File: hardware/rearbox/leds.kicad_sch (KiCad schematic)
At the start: 16 parts

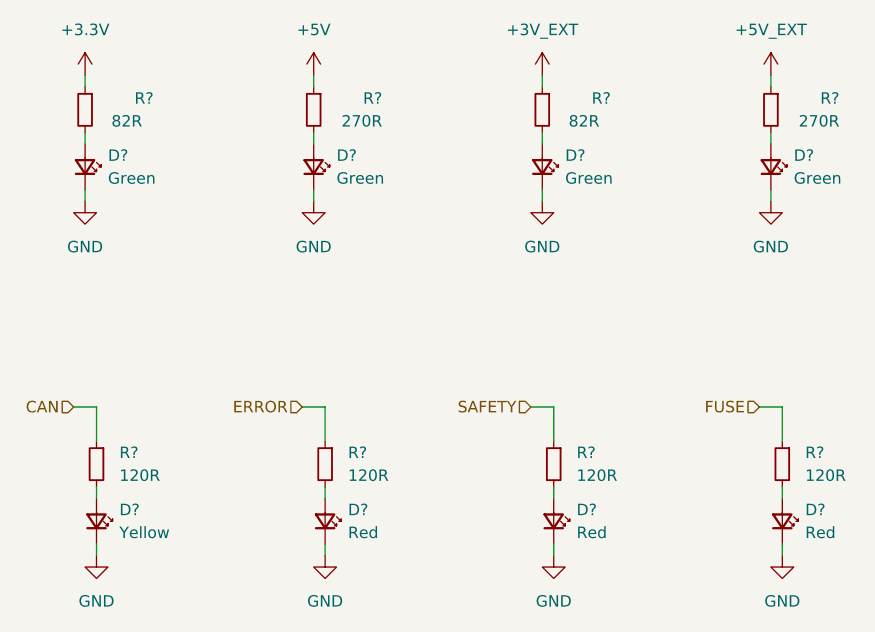
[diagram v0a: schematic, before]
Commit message: Place components on the PCB
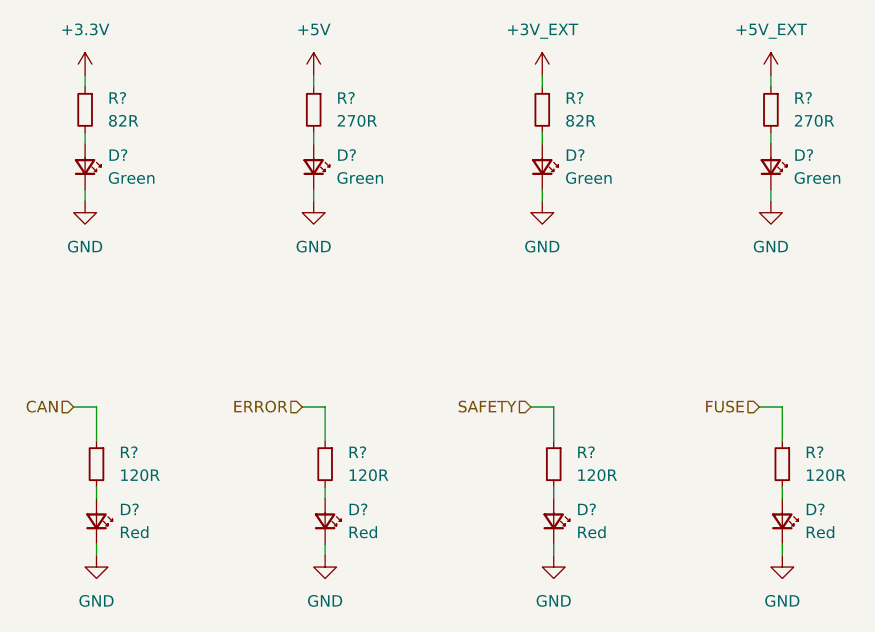
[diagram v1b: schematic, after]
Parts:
- D?: value Yellow -> Red
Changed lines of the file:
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@@
   (title_block
     (title "LEDs")
-    (date "2023-10-01")
+    (date "2023-11-02")
     (rev "${REVISION}")
     (company "Author: I. Kajdan")
@@
         )
         (path "/b652b05a-4e3d-4ad1-b032-18886abe7d45/6999686b-4026-4ea7-9227-634603a79198"
-          (reference "#PWR098") (unit 1)
+          (reference "#PWR095") (unit 1)
         )
       )
@@
         )
         (path "/b652b05a-4e3d-4ad1-b032-18886abe7d45/6999686b-4026-4ea7-9227-634603a79198"
-          (reference "#PWR099") (unit 1)
+          (reference "#PWR096") (unit 1)
         )
       )
@@
         )
         (path "/b652b05a-4e3d-4ad1-b032-18886abe7d45/6999686b-4026-4ea7-9227-634603a79198"
-          (reference "#PWR0106") (unit 1)
+          (reference "#PWR0103") (unit 1)
         )
       )
@@
         )
         (path "/b652b05a-4e3d-4ad1-b032-18886abe7d45/6999686b-4026-4ea7-9227-634603a79198"
-          (reference "R61") (unit 1)
+          (reference "R35") (unit 1)
         )
       )
@@
   (symbol (lib_id "Device:R_Small") (at 186.69 76.2 0) (mirror y) (unit 1)
     (in_bom yes) (on_board yes) (dnp no)
-    (property "Reference" "R?" (at 194.31 74.93 0)
-      (effects (font (size 1.27 1.27)) (justify left))
-    )
-    (property "Value" "270R" (at 194.31 77.47 0)
-      (effects (font (size 1.27 1.27)) (justify left))
+    (property "Reference" "R?" (at 189.23 74.93 0)
+      (effects (font (size 1.27 1.27)) (justify right))
+    )
+    (property "Value" "270R" (at 189.23 77.47 0)
+      (effects (font (size 1.27 1.27)) (justify right))
     )
     (property "Footprint" "Resistor_SMD:R_0603_1608Metric" (at 186.69 76.2 0)
@@
         )
         (path "/b652b05a-4e3d-4ad1-b032-18886abe7d45/6999686b-4026-4ea7-9227-634603a79198"
-          (reference "R66") (unit 1)
+          (reference "R40") (unit 1)
         )
       )
@@
       (effects (font (size 1.27 1.27)) (justify left))
     )
-    (property "Value" "Yellow" (at 114.3 123.19 90)
+    (property "Value" "Red" (at 114.3 123.19 90)
       (effects (font (size 1.27 1.27)) (justify left))
     )
@@
   (symbol (lib_id "Device:R_Small") (at 110.49 76.2 0) (mirror y) (unit 1)
     (in_bom yes) (on_board yes) (dnp no)
-    (property "Reference" "R?" (at 118.11 74.93 0)
-      (effects (font (size 1.27 1.27)) (justify left))
-    )
-    (property "Value" "82R" (at 116.84 77.47 0)
-      (effects (font (size 1.27 1.27)) (justify left))
+    (property "Reference" "R?" (at 113.03 74.93 0)
+      (effects (font (size 1.27 1.27)) (justify right))
+    )
+    (property "Value" "82R" (at 113.03 77.47 0)
+      (effects (font (size 1.27 1.27)) (justify right))
     )
     (property "Footprint" "Resistor_SMD:R_0603_1608Metric" (at 110.49 76.2 0)
@@
         )
         (path "/b652b05a-4e3d-4ad1-b032-18886abe7d45/6999686b-4026-4ea7-9227-634603a79198"
-          (reference "R60") (unit 1)
+          (reference "R34") (unit 1)
         )
       )
@@
         )
         (path "/b652b05a-4e3d-4ad1-b032-18886abe7d45/6999686b-4026-4ea7-9227-634603a79198"
-          (reference "#PWR096") (unit 1)
+          (reference "#PWR093") (unit 1)
         )
       )
@@
   (symbol (lib_id "Device:R_Small") (at 135.89 76.2 0) (mirror y) (unit 1)
     (in_bom yes) (on_board yes) (dnp no)
-    (property "Reference" "R?" (at 143.51 74.93 0)
-      (effects (font (size 1.27 1.27)) (justify left))
-    )
-    (property "Value" "270R" (at 143.51 77.47 0)
-      (effects (font (size 1.27 1.27)) (justify left))
+    (property "Reference" "R?" (at 138.43 74.93 0)
+      (effects (font (size 1.27 1.27)) (justify right))
+    )
+    (property "Value" "270R" (at 138.43 77.47 0)
+      (effects (font (size 1.27 1.27)) (justify right))
     )
     (property "Footprint" "Resistor_SMD:R_0603_1608Metric" (at 135.89 76.2 0)
@@
         )
         (path "/b652b05a-4e3d-4ad1-b032-18886abe7d45/6999686b-4026-4ea7-9227-634603a79198"
-          (reference "R62") (unit 1)
+          (reference "R36") (unit 1)
         )
       )
@@
         )
         (path "/b652b05a-4e3d-4ad1-b032-18886abe7d45/6999686b-4026-4ea7-9227-634603a79198"
-          (reference "#PWR0107") (unit 1)
+          (reference "#PWR0104") (unit 1)
         )
       )
@@
         )
         (path "/b652b05a-4e3d-4ad1-b032-18886abe7d45/6999686b-4026-4ea7-9227-634603a79198"
-          (reference "#PWR0101") (unit 1)
+          (reference "#PWR098") (unit 1)
         )
       )
@@
         )
         (path "/b652b05a-4e3d-4ad1-b032-18886abe7d45/6999686b-4026-4ea7-9227-634603a79198"
-          (reference "#PWR097") (unit 1)
+          (reference "#PWR094") (unit 1)
         )
       )
@@
         )
         (path "/b652b05a-4e3d-4ad1-b032-18886abe7d45/6999686b-4026-4ea7-9227-634603a79198"
-          (reference "R67") (unit 1)
+          (reference "R41") (unit 1)
         )
       )
@@
         )
         (path "/b652b05a-4e3d-4ad1-b032-18886abe7d45/6999686b-4026-4ea7-9227-634603a79198"
-          (reference "R63") (unit 1)
+          (reference "R37") (unit 1)
         )
       )
@@
         )
         (path "/b652b05a-4e3d-4ad1-b032-18886abe7d45/6999686b-4026-4ea7-9227-634603a79198"
-          (reference "R65") (unit 1)
+          (reference "R39") (unit 1)
         )
       )
@@
   (symbol (lib_id "Power_Ports:+3V_EXT") (at 161.29 72.39 0) (unit 1)
     (in_bom yes) (on_board yes) (dnp no) (fields_autoplaced)
-    (property "Reference" "#PWR0102" (at 167.64 72.39 0)
+    (property "Reference" "#PWR099" (at 167.64 72.39 0)
       (effects (font (size 1.27 1.27)) hide)
     )
@@
       (project "rearbox"
         (path "/b652b05a-4e3d-4ad1-b032-18886abe7d45/6999686b-4026-4ea7-9227-634603a79198"
-          (reference "#PWR0102") (unit 1)
+          (reference "#PWR099") (unit 1)
         )
       )
@@
         )
         (path "/b652b05a-4e3d-4ad1-b032-18886abe7d45/6999686b-4026-4ea7-9227-634603a79198"
-          (reference "#PWR0104") (unit 1)
+          (reference "#PWR0101") (unit 1)
         )
       )
@@
   (symbol (lib_id "Device:R_Small") (at 161.29 76.2 0) (mirror y) (unit 1)
     (in_bom yes) (on_board yes) (dnp no)
-    (property "Reference" "R?" (at 168.91 74.93 0)
-      (effects (font (size 1.27 1.27)) (justify left))
-    )
-    (property "Value" "82R" (at 167.64 77.47 0)
-      (effects (font (size 1.27 1.27)) (justify left))
+    (property "Reference" "R?" (at 163.83 74.93 0)
+      (effects (font (size 1.27 1.27)) (justify right))
+    )
+    (property "Value" "82R" (at 163.83 77.47 0)
+      (effects (font (size 1.27 1.27)) (justify right))
     )
     (property "Footprint" "Resistor_SMD:R_0603_1608Metric" (at 161.29 76.2 0)
@@
         )
         (path "/b652b05a-4e3d-4ad1-b032-18886abe7d45/6999686b-4026-4ea7-9227-634603a79198"
-          (reference "R64") (unit 1)
+          (reference "R38") (unit 1)
         )
       )
@@
           (reference "#PWR051") (unit 1)
         )
-        (path "/b652b05a-4e3d-4ad1-b032-18886abe7d45/620acd23-76d3-49a1-9dab-637cd753e552/d07b630f-4126-4aee-9634-5a26ef1ba4a0"
-          (reference "#PWR0221") (unit 1)
-        )
-        (path "/b652b05a-4e3d-4ad1-b032-18886abe7d45/620acd23-76d3-49a1-9dab-637cd753e552/748a5b35-762a-4e72-b9b9-898b09e1f3d2"
-          (reference "#PWR0232") (unit 1)
-        )
-        (path "/b652b05a-4e3d-4ad1-b032-18886abe7d45/6999686b-4026-4ea7-9227-634603a79198"
-          (reference "#PWR0105") (unit 1)
+        (path "/b652b05a-4e3d-4ad1-b032-18886abe7d45/6999686b-4026-4ea7-9227-634603a79198"
+          (reference "#PWR0102") (unit 1)
         )
       )
@@
         )
         (path "/b652b05a-4e3d-4ad1-b032-18886abe7d45/6999686b-4026-4ea7-9227-634603a79198"
+          (reference "#PWR097") (unit 1)
+        )
+      )
+    )
+  )
+  (symbol (lib_id "power:GND") (at 161.29 86.36 0) (unit 1)
+    (in_bom yes) (on_board yes) (dnp no)
+    (property "Reference" "#PWR?" (at 161.29 92.71 0)
+      (effects (font (size 1.27 1.27)) hide)
+    )
+    (property "Value" "GND" (at 161.29 91.44 0)
+      (effects (font (size 1.27 1.27)))
+    )
+    (property "Footprint" "" (at 161.29 86.36 0)
+      (effects (font (size 1.27 1.27)) hide)
+    )
+    (property "Datasheet" "" (at 161.29 86.36 0)
+      (effects (font (size 1.27 1.27)) hide)
+    )
+    (pin "1")
+    (instances
+      (project "rearbox"
+        (path "/b652b05a-4e3d-4ad1-b032-18886abe7d45/7045152e-d7a2-42d7-9b15-138e7f2928ca"
+          (reference "#PWR?") (unit 1)
+        )
+        (path "/b652b05a-4e3d-4ad1-b032-18886abe7d45"
+          (reference "#PWR?") (unit 1)
+        )
+        (path "/b652b05a-4e3d-4ad1-b032-18886abe7d45/6999686b-4026-4ea7-9227-634603a79198"
           (reference "#PWR0100") (unit 1)
         )
       )
-    )
-  )
-  (symbol (lib_id "power:GND") (at 161.29 86.36 0) (unit 1)
-    (in_bom yes) (on_board yes) (dnp no)
-    (property "Reference" "#PWR?" (at 161.29 92.71 0)
-      (effects (font (size 1.27 1.27)) hide)
-    )
-    (property "Value" "GND" (at 161.29 91.44 0)
-      (effects (font (size 1.27 1.27)))
-    )
-    (property "Footprint" "" (at 161.29 86.36 0)
-      (effects (font (size 1.27 1.27)) hide)
-    )
-    (property "Datasheet" "" (at 161.29 86.36 0)
-      (effects (font (size 1.27 1.27)) hide)
-    )
-    (pin "1")
-    (instances
-      (project "rearbox"
-        (path "/b652b05a-4e3d-4ad1-b032-18886abe7d45/7045152e-d7a2-42d7-9b15-138e7f2928ca"
-          (reference "#PWR?") (unit 1)
-        )
-        (path "/b652b05a-4e3d-4ad1-b032-18886abe7d45"
-          (reference "#PWR?") (unit 1)
-        )
-        (path "/b652b05a-4e3d-4ad1-b032-18886abe7d45/6999686b-4026-4ea7-9227-634603a79198"
-          (reference "#PWR0103") (unit 1)
-        )
-      )

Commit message: Align footprint references
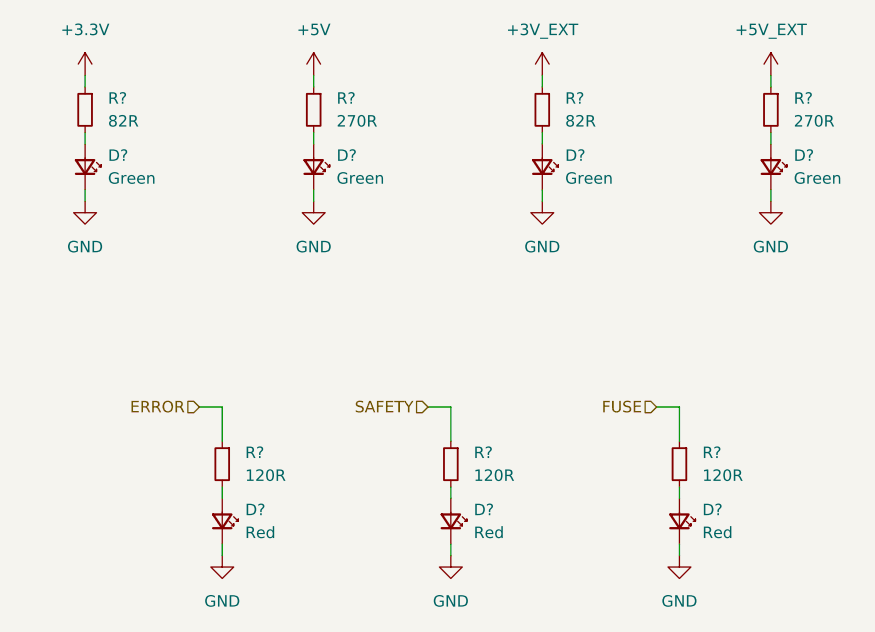
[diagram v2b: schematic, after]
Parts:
- removed D?: Red, LED_SMD:LED_0603_1608Metric, symbol Device:LED_Small
- removed R?: 120R, Resistor_SMD:R_0603_1608Metric, symbol Device:R_Small
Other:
- moved on the sheet: D?, R?

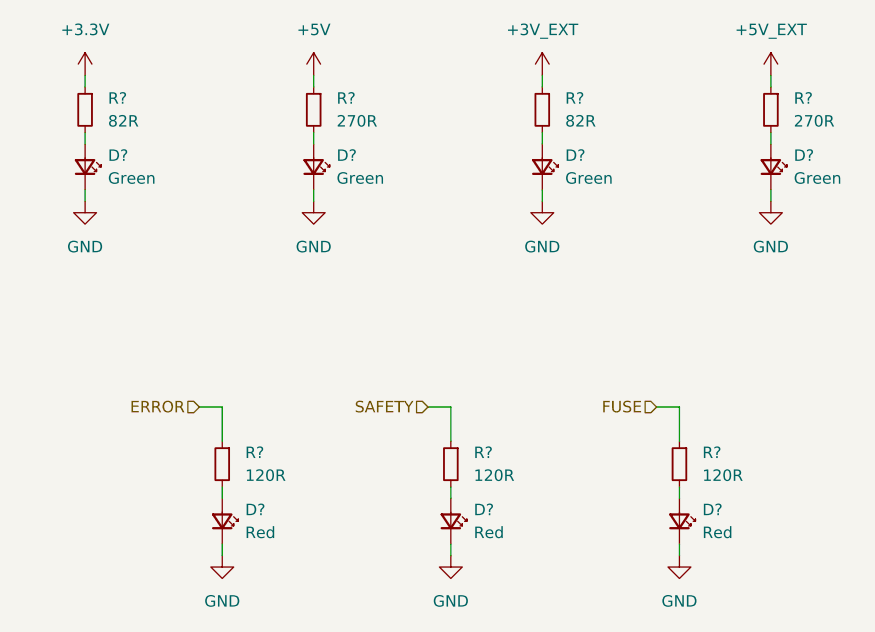
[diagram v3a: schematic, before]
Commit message: Route the tracks on the connector PCB
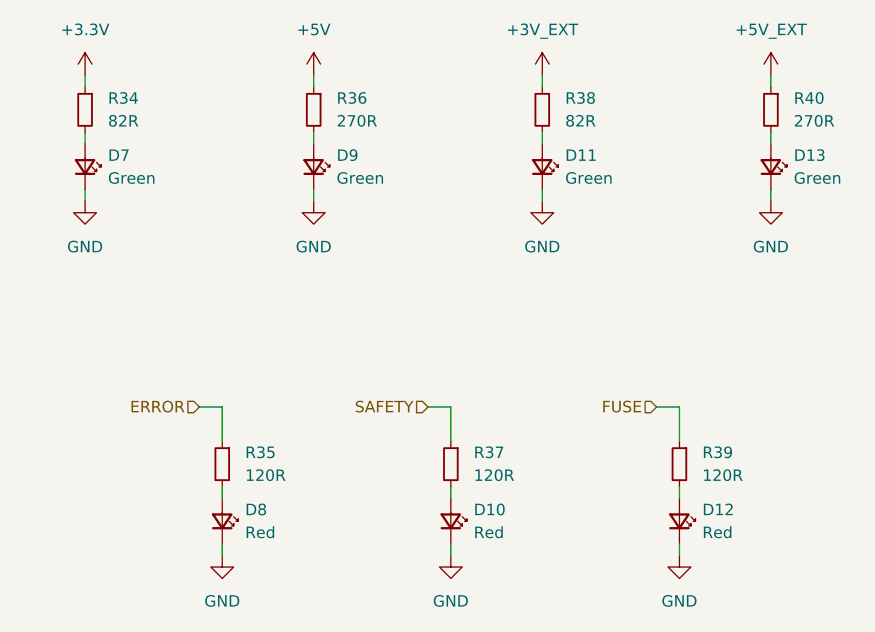
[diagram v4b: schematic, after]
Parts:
- gave numbers to parts that had none: 14

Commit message: Fix measurement bridges polarity
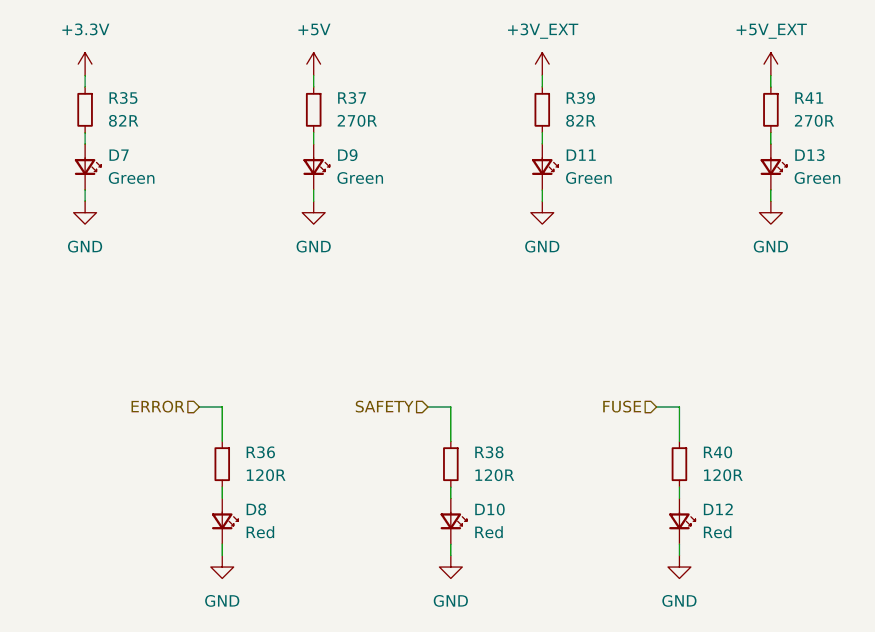
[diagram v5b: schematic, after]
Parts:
- renumbered R34 to R35, R35 to R36, R36 to R37, R37 to R38, R38 to R39, R39 to R40, R40 to R41
